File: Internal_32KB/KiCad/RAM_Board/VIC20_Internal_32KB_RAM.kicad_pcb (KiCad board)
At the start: 2 copper layers, 65.8 x 64 mm, 13 parts, among them J1 UD4, J2 UE4, J3 Switch, J4 RAM Decode, J5 BLK Inputs, J6 BLK Outputs, U1 62256, U2 RAM Decoder, U3 BLK Decoder

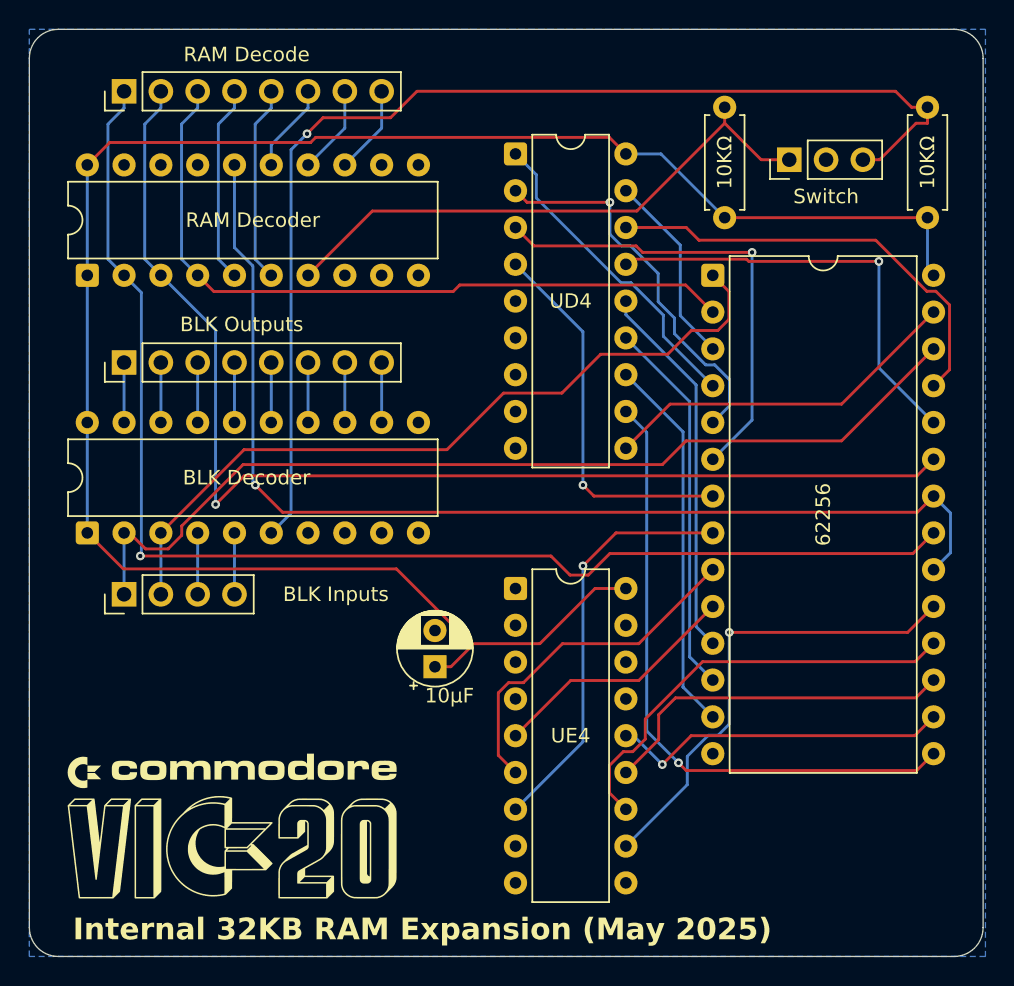
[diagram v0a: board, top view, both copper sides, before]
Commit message: Finalising RAM board design
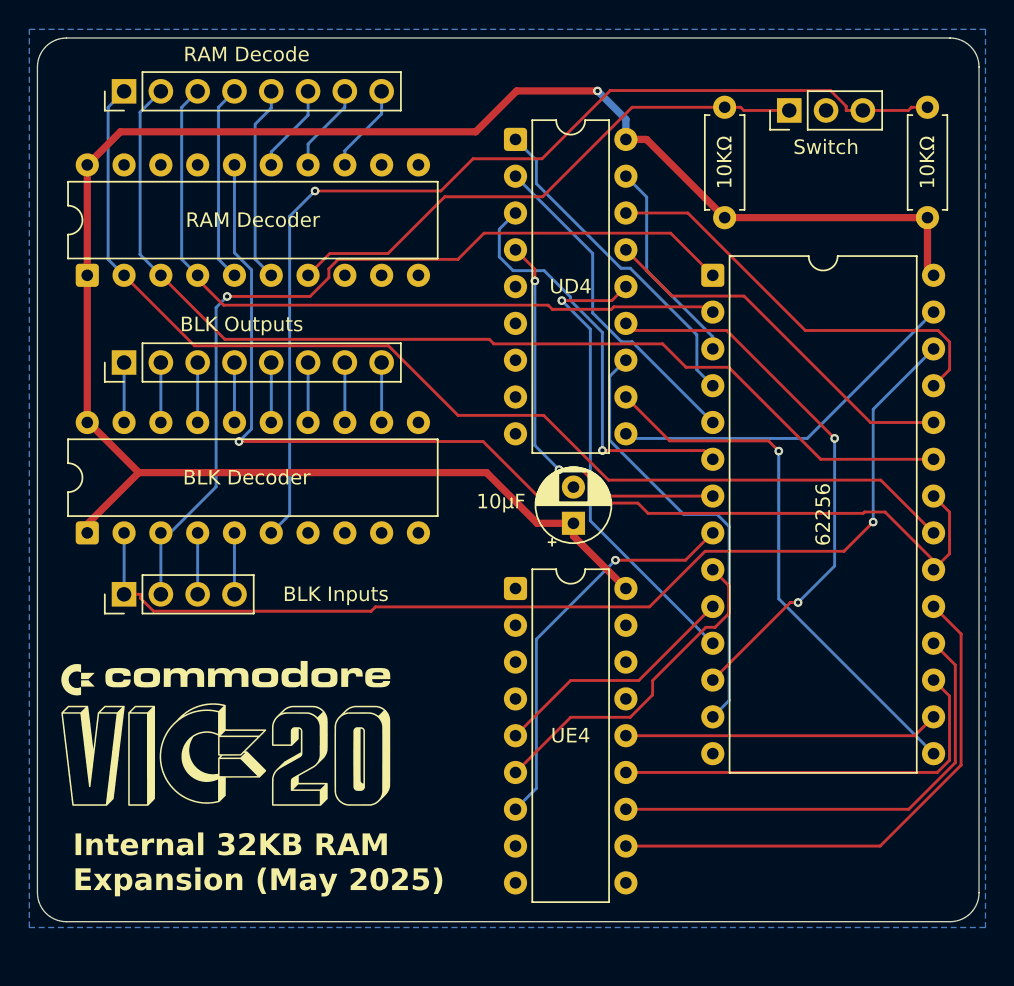
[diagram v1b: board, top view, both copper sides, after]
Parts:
- moved C1 13.8 mm to (84.0, 61.6)
- moved G*** 6.42 mm to (60.0, 76.1)
- moved J3 3.40 mm to (98.9, 33.1)
- moved J1 1.00 mm to (80.0, 35.1)
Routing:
- net VA10: track 90.0 -> 76.9 mm, vias 1 -> 0
- net BD1: track 26.1 -> 38.2 mm, vias 0 -> 2
- net VA11: track 81.9 -> 72.5 mm, vias 1 -> 0
- net S2: track 79.7 -> 70.8 mm
- net CA14: track 53.1 -> 60.0 mm, vias 0 -> 1
- net BD0: track 26.1 -> 32.8 mm, vias 0 -> 1
- net BD3: track 44.1 -> 37.4 mm
- net CA13: track 66.7 -> 72.8 mm, vias 0 -> 1
- net BD7: track 32.9 -> 37.2 mm, vias 1 -> 0
- net BD2: track 26.1 -> 30.3 mm
- net VA9: track 30.4 -> 26.2 mm, vias 1 -> 0
- net BD5: track 24.9 -> 28.7 mm
- net VA5: track 26.7 -> 23.1 mm, vias 1 -> 0
- net VA4: track 32.4 -> 28.9 mm
- net BD6: track 30.2 -> 32.9 mm
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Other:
- board size 65.8 x 64 mm -> 65 x 61 mm

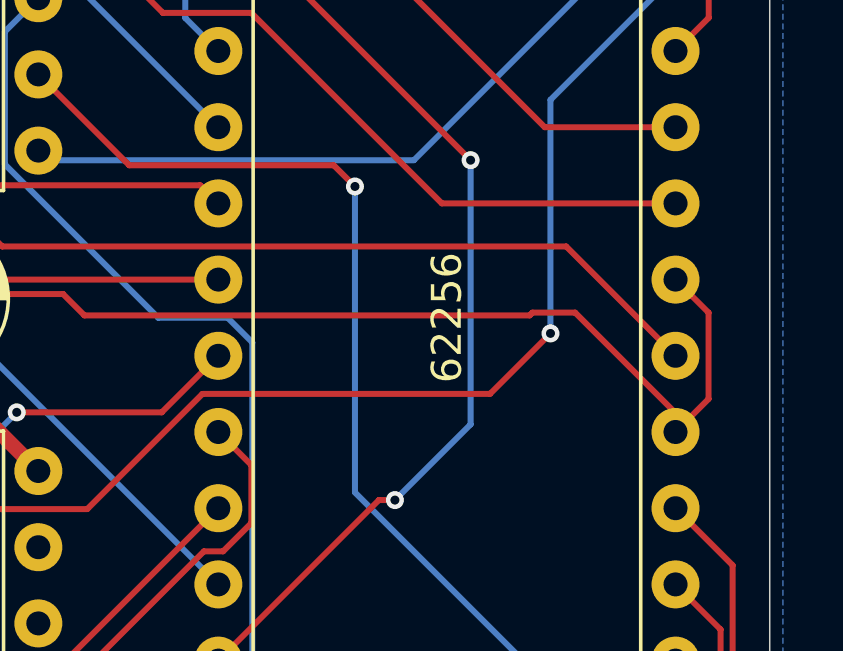
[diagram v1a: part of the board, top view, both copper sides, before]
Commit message: Sent for test fabrication
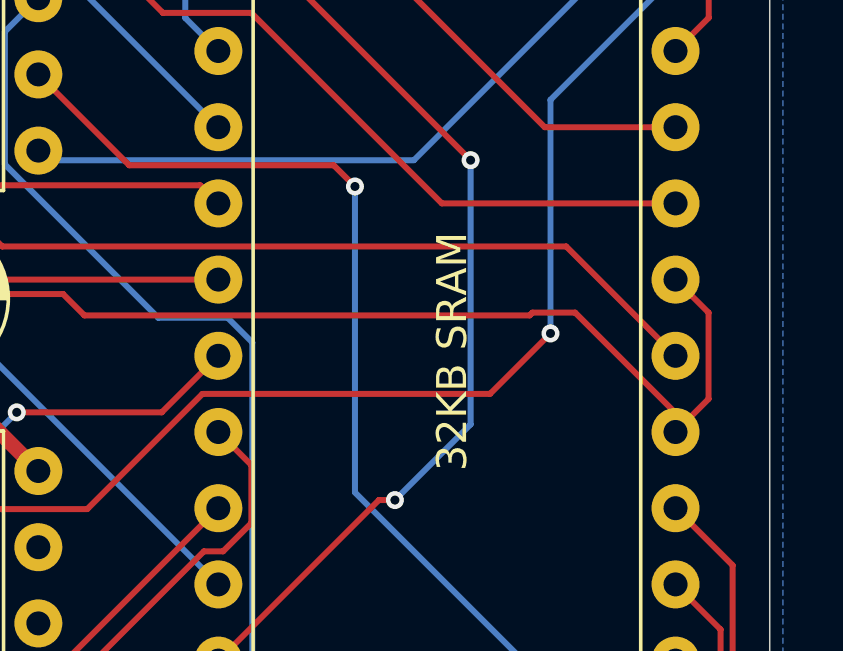
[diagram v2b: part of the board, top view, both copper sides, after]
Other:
- board text added: "32KB SRAM"
- board text added: "Brett Hallen, May 2025 Port Macquarie, Australia www.youtube.com/@Brfff"
- board text removed: "Brett Hallen, Apr 2025 Port Macquarie, Australia www.youtube.com/@Brfff"
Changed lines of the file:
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@@
 			(at 7.62 16.51 90)
 			(layer "F.SilkS")
+			(hide yes)
 			(effects
 				(font
@@
 		)
 	)
-	(gr_text "Brett Hallen, Apr 2025\nPort Macquarie, Australia\nwww.youtube.com/@Brfff"
-		(at 118.04 39.12 0)
+	(gr_text "32KB SRAM"
+		(at 102.04 66.12 90)
+		(layer "F.SilkS")
+		(effects
+			(font
+				(size 1 1)
+				(thickness 0.15)
+			)
+			(justify left bottom)
+		)
+	)
+	(gr_text "Brett Hallen, May 2025\nPort Macquarie, Australia\nwww.youtube.com/@Brfff"
+		(at 78.04 87.12 0)
 		(layer "B.SilkS")
 		(effects
